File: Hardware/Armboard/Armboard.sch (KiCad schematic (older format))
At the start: 24 parts

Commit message: Added more footprints
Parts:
- Conn1, Conn2: footprint (none) -> MRDT_Connectors:Anderson_1_Horizontal
- Conn3, Conn4, Conn5: footprint (none) -> MRDT_Connectors:Anderson_3_Vertical_Side_by_Side
- Conn6, Conn7: footprint (none) -> MRDT_Connectors:Anderson_2_Vertical_Sidy_by_Side
- D2, D3, D4, D5, D6, D7: footprint (none) -> LED_SMD:LED_0603_1608Metric_Pad1.05x0.95mm_HandSolder
- FB1, FB2, FB3, FB4, FB5: footprint (none) -> Capacitor_SMD:C_0805_2012Metric_Pad1.15x1.40mm_HandSolder
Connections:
- net Power/12V is gone; now on net Power/12V: Conn2.2 (V+Log), Conn3.2 (V+Log), Conn4.2 (V+Log), Conn5.2 (V+Log)
- net Power/12V: no longer FB1.2, FB2.2, FB3.2
- new net Power/12V: FB1.2, FB2.2, FB3.2
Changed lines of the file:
@@
 F 0 "Conn1" H 1843 1737 60  0000 C CNN
 F 1 "AndersonPP" H 1843 1631 60  0000 C CNN
-F 2 "" H 1485 800 60  0001 C CNN
+F 2 "MRDT_Connectors:Anderson_1_Horizontal" H 1485 800 60  0001 C CNN
 F 3 "" H 1485 800 60  0001 C CNN
 	3    1635 1350
@@
 F 0 "D2" H 9608 1357 50  0000 C CNN
 F 1 "LED" H 9608 1266 50  0000 C CNN
-F 2 "" H 9615 1520 50  0001 C CNN
+F 2 "LED_SMD:LED_0603_1608Metric_Pad1.05x0.95mm_HandSolder" H 9615 1520 50  0001 C CNN
 F 3 "~" H 9615 1520 50  0001 C CNN
 	1    9615 1520
@@
 F 0 "Conn6" H 10340 1750 60  0000 R CNN
 F 1 "AndersonPP" H 10440 1650 60  0000 R CNN
-F 2 "" H 9890 800 60  0001 C CNN
+F 2 "MRDT_Connectors:Anderson_2_Vertical_Sidy_by_Side" H 9890 800 60  0001 C CNN
 F 3 "" H 9890 800 60  0001 C CNN
 	2    10040 1350
@@
 F 0 "D6" H 4718 1140 50  0000 C CNN
 F 1 "LED" H 4718 1231 50  0000 C CNN
-F 2 "" H 4725 1395 50  0001 C CNN
+F 2 "LED_SMD:LED_0603_1608Metric_Pad1.05x0.95mm_HandSolder" H 4725 1395 50  0001 C CNN
 F 3 "~" H 4725 1395 50  0001 C CNN
 	1    4725 1395
@@
 F 0 "Conn3" H 1425 2950 60  0000 C CNN
 F 1 "AndersonPP" H 1330 2840 60  0000 C CNN
-F 2 "" H 1485 2240 60  0001 C CNN
+F 2 "MRDT_Connectors:Anderson_3_Vertical_Side_by_Side" H 1485 2240 60  0001 C CNN
 F 3 "" H 1485 2240 60  0001 C CNN
 	1    1635 2790
@@
 F 0 "Conn4" H 1425 3175 60  0000 C CNN
 F 1 "AndersonPP" H 1330 3065 60  0000 C CNN
-F 2 "" H 1485 2465 60  0001 C CNN
+F 2 "MRDT_Connectors:Anderson_3_Vertical_Side_by_Side" H 1485 2465 60  0001 C CNN
 F 3 "" H 1485 2465 60  0001 C CNN
 	1    1635 3015
@@
 F 0 "Conn5" H 1425 3400 60  0000 C CNN
 F 1 "AndersonPP" H 1330 3290 60  0000 C CNN
-F 2 "" H 1485 2690 60  0001 C CNN
+F 2 "MRDT_Connectors:Anderson_3_Vertical_Side_by_Side" H 1485 2690 60  0001 C CNN
 F 3 "" H 1485 2690 60  0001 C CNN
 	1    1635 3240
@@
 F 0 "Conn2" H 1425 2725 60  0000 C CNN
 F 1 "AndersonPP" H 1330 2615 60  0000 C CNN
-F 2 "" H 1485 2015 60  0001 C CNN
+F 2 "MRDT_Connectors:Anderson_1_Horizontal" H 1485 2015 60  0001 C CNN
 F 3 "" H 1485 2015 60  0001 C CNN
 	1    1635 2565
@@
 F 0 "FB4" V 8898 1250 50  0000 C CNN
 F 1 "Ferrite_Bead_Small" V 8989 1250 50  0000 C CNN
-F 2 "" V 9065 1250 50  0001 C CNN
+F 2 "Capacitor_SMD:C_0805_2012Metric_Pad1.15x1.40mm_HandSolder" V 9065 1250 50  0001 C CNN
 F 3 "~" H 9135 1250 50  0001 C CNN
 	1    9135 1250
@@
 F 0 "D7" H 9728 2407 50  0000 C CNN
 F 1 "LED" H 9728 2316 50  0000 C CNN
-F 2 "" H 9735 2570 50  0001 C CNN
+F 2 "LED_SMD:LED_0603_1608Metric_Pad1.05x0.95mm_HandSolder" H 9735 2570 50  0001 C CNN
 F 3 "~" H 9735 2570 50  0001 C CNN
 	1    9735 2570
@@
 F 0 "Conn7" H 10480 2800 60  0000 R CNN
 F 1 "AndersonPP" H 10580 2700 60  0000 R CNN
-F 2 "" H 10030 1850 60  0001 C CNN
+F 2 "MRDT_Connectors:Anderson_2_Vertical_Sidy_by_Side" H 10030 1850 60  0001 C CNN
 F 3 "" H 10030 1850 60  0001 C CNN
 	2    10180 2400
@@
 F 0 "FB5" V 9038 2300 50  0000 C CNN
 F 1 "Ferrite_Bead_Small" V 9129 2300 50  0000 C CNN
-F 2 "" V 9205 2300 50  0001 C CNN
+F 2 "Capacitor_SMD:C_0805_2012Metric_Pad1.15x1.40mm_HandSolder" V 9205 2300 50  0001 C CNN
 F 3 "~" H 9275 2300 50  0001 C CNN
 	1    9275 2300
@@
 F 0 "FB1" V 4125 1805 30  0000 C CNN
 F 1 "Ferrite_Bead_Small" V 4190 1805 30  0000 C CNN
-F 2 "" V 4225 1805 50  0001 C CNN
+F 2 "Capacitor_SMD:C_0805_2012Metric_Pad1.15x1.40mm_HandSolder" V 4225 1805 50  0001 C CNN
 F 3 "~" H 4295 1805 50  0001 C CNN
 	1    4295 1805
@@
 F 0 "D3" H 4715 2150 30  0000 C CNN
 F 1 "LED" H 4630 2150 30  0000 C CNN
-F 2 "" H 4655 2005 50  0001 C CNN
+F 2 "LED_SMD:LED_0603_1608Metric_Pad1.05x0.95mm_HandSolder" H 4655 2005 50  0001 C CNN
 F 3 "~" H 4655 2005 50  0001 C CNN
 	1    4655 2005
@@
 F 0 "Conn2" H 4962 1752 60  0000 R CNN
 F 1 "AndersonPP" H 4962 1858 60  0000 R CNN
-F 2 "" H 4840 1155 60  0001 C CNN
+F 2 "MRDT_Connectors:Anderson_1_Horizontal" H 4840 1155 60  0001 C CNN
 F 3 "" H 4840 1155 60  0001 C CNN
 	3    4990 1705
@@
 F 0 "FB2" V 4175 2265 30  0000 C CNN
 F 1 "Ferrite_Bead_Small" V 4225 2310 30  0000 C CNN
-F 2 "" V 4255 2220 50  0001 C CNN
+F 2 "Capacitor_SMD:C_0805_2012Metric_Pad1.15x1.40mm_HandSolder" V 4255 2220 50  0001 C CNN
 F 3 "~" H 4325 2220 50  0001 C CNN
 	1    4325 2220
@@
 F 0 "D4" H 4685 2555 30  0000 C CNN
 F 1 "LED" H 4685 2320 30  0000 C CNN
-F 2 "" H 4685 2420 50  0001 C CNN
+F 2 "LED_SMD:LED_0603_1608Metric_Pad1.05x0.95mm_HandSolder" H 4685 2420 50  0001 C CNN
 F 3 "~" H 4685 2420 50  0001 C CNN
 	1    4685 2420
@@
 F 0 "Conn3" H 4992 2167 60  0000 R CNN
 F 1 "AndersonPP" H 4992 2273 60  0000 R CNN
-F 2 "" H 4870 1570 60  0001 C CNN
+F 2 "MRDT_Connectors:Anderson_3_Vertical_Side_by_Side" H 4870 1570 60  0001 C CNN
 F 3 "" H 4870 1570 60  0001 C CNN
 	3    5020 2120
@@
 F 0 "FB3" V 4175 2725 30  0000 C CNN
 F 1 "Ferrite_Bead_Small" V 4225 2770 30  0000 C CNN
-F 2 "" V 4255 2680 50  0001 C CNN
+F 2 "Capacitor_SMD:C_0805_2012Metric_Pad1.15x1.40mm_HandSolder" V 4255 2680 50  0001 C CNN
 F 3 "~" H 4325 2680 50  0001 C CNN
 	1    4325 2680
@@
 F 0 "D5" H 4685 3015 30  0000 C CNN
 F 1 "LED" H 4685 2780 30  0000 C CNN
-F 2 "" H 4685 2880 50  0001 C CNN
+F 2 "LED_SMD:LED_0603_1608Metric_Pad1.05x0.95mm_HandSolder" H 4685 2880 50  0001 C CNN
 F 3 "~" H 4685 2880 50  0001 C CNN
 	1    4685 2880
@@
 F 0 "Conn4" H 4992 2627 60  0000 R CNN
 F 1 "AndersonPP" H 4992 2733 60  0000 R CNN
-F 2 "" H 4870 2030 60  0001 C CNN
+F 2 "MRDT_Connectors:Anderson_3_Vertical_Side_by_Side" H 4870 2030 60  0001 C CNN
 F 3 "" H 4870 2030 60  0001 C CNN
 	3    5020 2580
@@
 F 0 "Conn2" H 1450 1750 60  0000 C CNN
 F 1 "AndersonPP" H 1355 1655 60  0000 C CNN
-F 2 "" H 1485 1060 60  0001 C CNN
+F 2 "MRDT_Connectors:Anderson_1_Horizontal" H 1485 1060 60  0001 C CNN
 F 3 "" H 1485 1060 60  0001 C CNN
 	2    1635 1610
@@
 F 0 "Conn3" H 1450 1975 60  0000 C CNN
 F 1 "AndersonPP" H 1355 1880 60  0000 C CNN
-F 2 "" H 1485 1285 60  0001 C CNN
+F 2 "MRDT_Connectors:Anderson_3_Vertical_Side_by_Side" H 1485 1285 60  0001 C CNN
 F 3 "" H 1485 1285 60  0001 C CNN
 	2    1635 1835
@@
 F 0 "Conn4" H 1450 2200 60  0000 C CNN
 F 1 "AndersonPP" H 1355 2105 60  0000 C CNN
-F 2 "" H 1485 1510 60  0001 C CNN
+F 2 "MRDT_Connectors:Anderson_3_Vertical_Side_by_Side" H 1485 1510 60  0001 C CNN
 F 3 "" H 1485 1510 60  0001 C CNN
 	2    1635 2060
@@
 F 0 "Conn5" H 1450 2425 60  0000 C CNN
 F 1 "AndersonPP" H 1355 2330 60  0000 C CNN
-F 2 "" H 1485 1735 60  0001 C CNN
+F 2 "MRDT_Connectors:Anderson_3_Vertical_Side_by_Side" H 1485 1735 60  0001 C CNN
 F 3 "" H 1485 1735 60  0001 C CNN
 	2    1635 2285

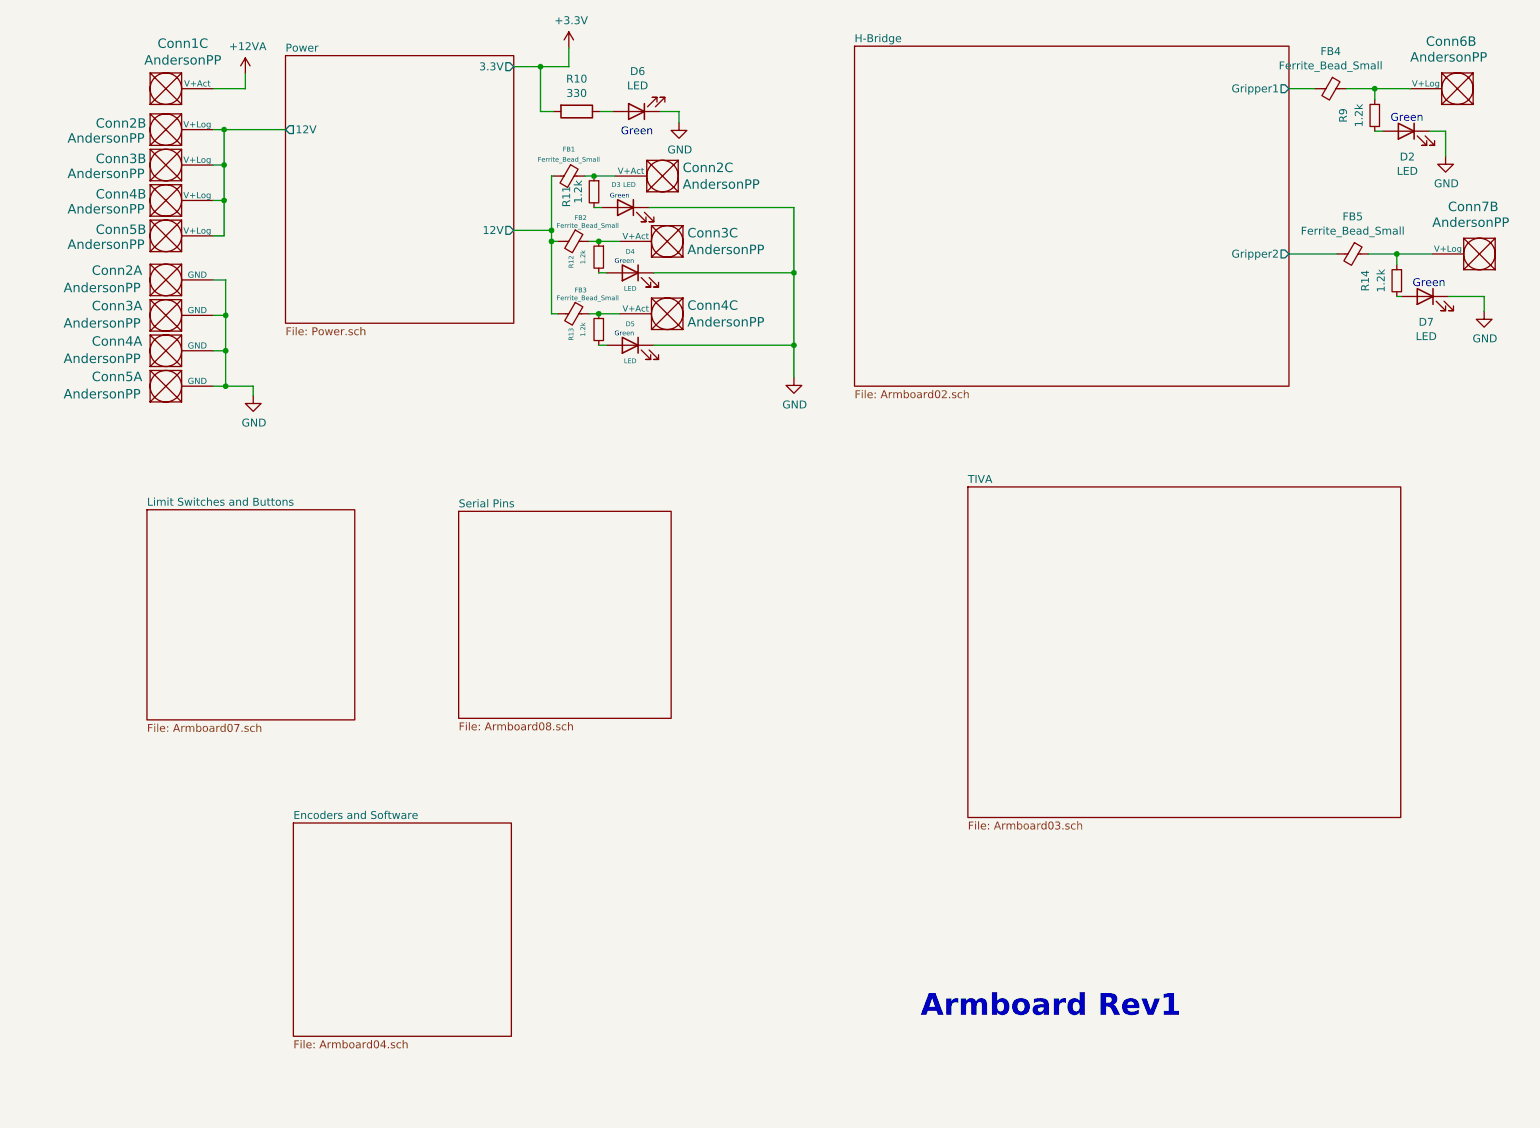
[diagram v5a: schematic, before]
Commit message: Fixed Andersons, made netlist, imported footprints to layout
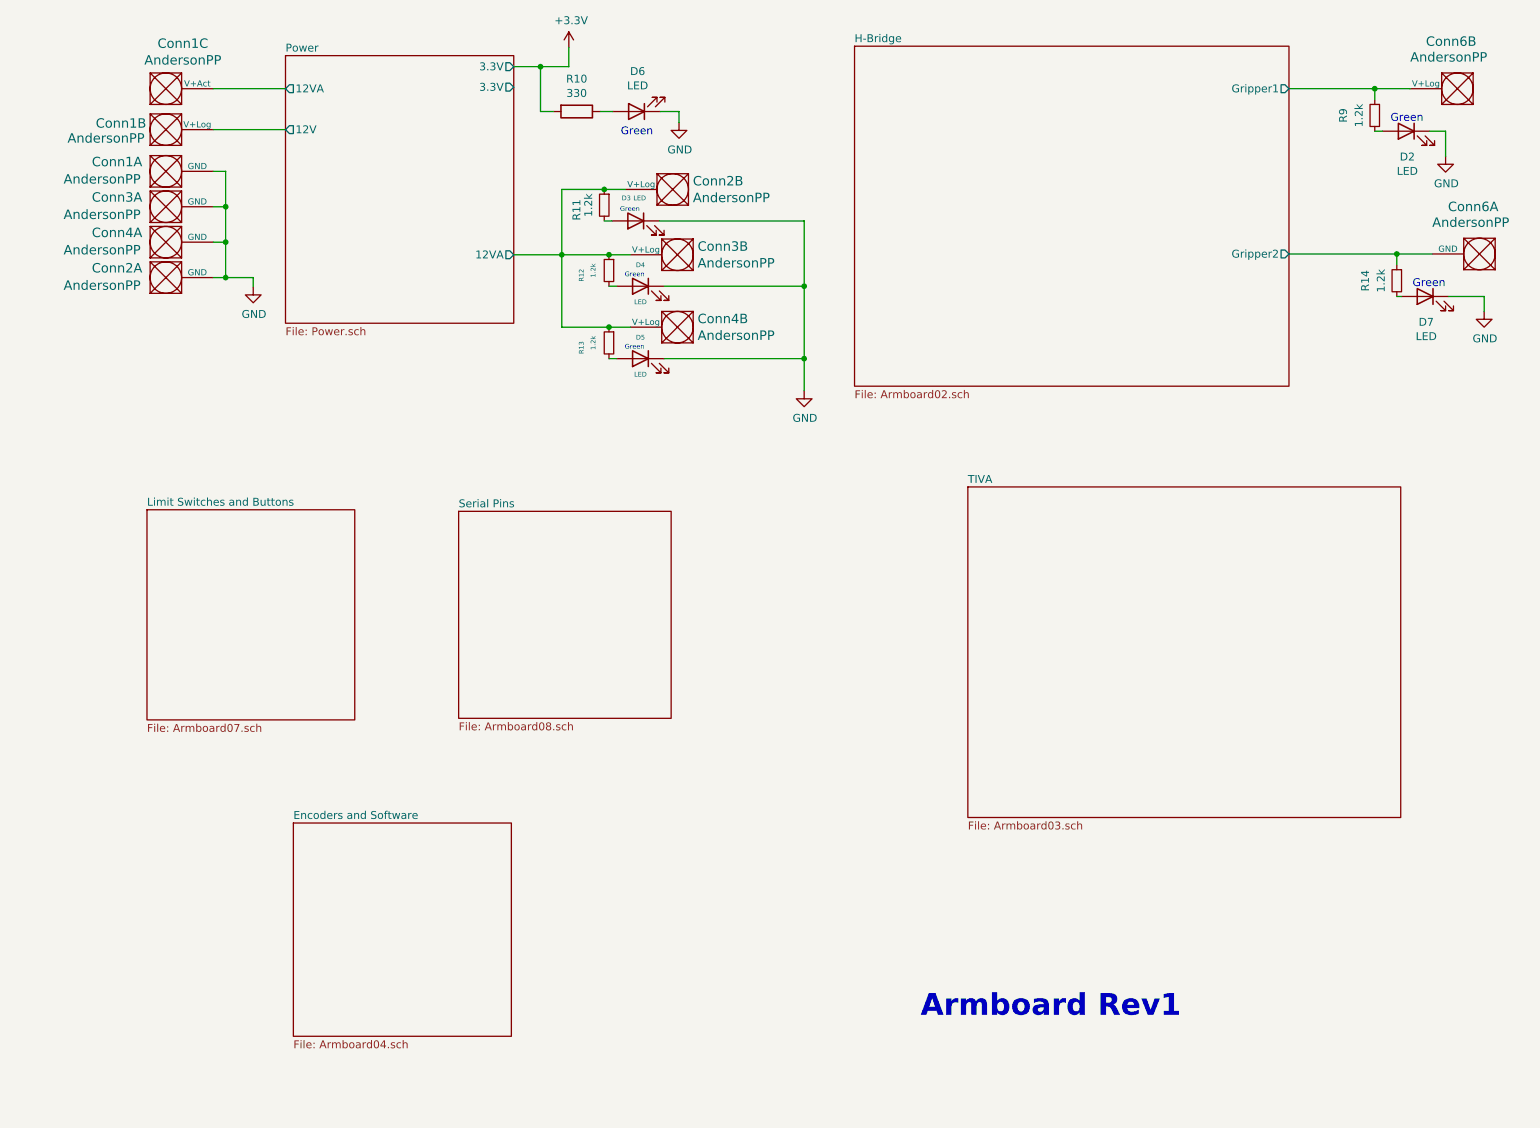
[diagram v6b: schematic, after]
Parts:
- removed unit 2 of Conn3
- removed unit 2 of Conn4
- removed unit 2 of Conn5
- removed FB1, FB2, FB3, FB4, FB5: Ferrite_Bead_Small, Capacitor_SMD:C_0805_2012Metric_Pad1.15x1.40mm_HandSolder, symbol Device:Ferrite_Bead_Small
- Conn1: footprint MRDT_Connectors:Anderson_1_Horizontal -> MRDT_Connectors:Anderson_3_Horizontal_Side_by_Side
- Conn1: renamed from Conn2; footprint MRDT_Connectors:Anderson_1_Horizontal -> MRDT_Connectors:Anderson_3_Horizontal_Side_by_Side
- Conn2: footprint MRDT_Connectors:Anderson_1_Horizontal -> MRDT_Connectors:Anderson_2_Vertical_Sidy_by_Side
- Conn2: renamed from Conn5; footprint MRDT_Connectors:Anderson_3_Vertical_Side_by_Side -> MRDT_Connectors:Anderson_2_Vertical_Sidy_by_Side
- Conn3, Conn4: footprint MRDT_Connectors:Anderson_3_Vertical_Side_by_Side -> MRDT_Connectors:Anderson_2_Vertical_Sidy_by_Side
- renumbered Conn7 to Conn6
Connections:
- net Power/12V is gone; now on net Power/12V: Conn1.2 (V+Log)
- net H-Bridge/Gripper1: now also Conn6.2 (V+Log), R9.1
- net H-Bridge/Gripper2: now also Conn6.1 (GND), R14.1
- net Power/12VA: now reaches R11.1
- net Power/12VA: now also Conn2.2 (V+Log), Conn3.2 (V+Log), Conn4.2 (V+Log), R12.1, R13.1; no longer Conn2.3 (V+Act)
- net +12VA renamed Power/12VA
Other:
- moved on the sheet: Conn1A, Conn2A, Conn3A, Conn4A, D3, D4, D5, R11, R12, R13

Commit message: Double-checked schematic, pointed power pins up, made sure 12V and 3.3V were full networks
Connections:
- net Power/12VA is gone; now on net Power/12VA: Conn2.2 (V+Log), Conn3.2 (V+Log), Conn4.2 (V+Log), R11.1, R12.1, R13.1
- net Power/12VA: no longer Conn1.3 (V+Act)
- new net Power/12VA: Conn1.3 (V+Act)
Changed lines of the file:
@@
 F0 "Power" 50
 F1 "Power.sch" 50
-F2 "3.3V" O R 3945 1240 50
-F3 "12V" O L 2495 1510 50
-F4 "12VA" O L 2495 1250 50
-F5 "12VA" O R 3945 2305 50
-F6 "3.3V" O R 3945 1110 50
+F2 "12V" O L 2495 1510 50
+F3 "12VA" O L 2495 1250 50
+F4 "12VA" O R 3945 2305 50
+F5 "3.3V" O R 3945 1110 50
+F6 "12V" O R 3945 1760 50
 $EndSheet
 $Comp
@@
 Wire Wire Line
 	3945 2305 4250 2305
+Wire Wire Line
+	3945 1760 4120 1760
+Wire Wire Line
+	4120 1760 4120 1705
+$Comp
+L power:+12V #PWR0101
+U 1 1 5FBDA204
+P 4120 1705
+F 0 "#PWR0101" H 4120 1555 50  0001 C CNN
+F 1 "+12V" H 4135 1878 50  0000 C CNN
+F 2 "" H 4120 1705 50  0001 C CNN
+F 3 "" H 4120 1705 50  0001 C CNN
+	1    4120 1705
+	1    0    0    -1
+$EndComp
 $EndSCHEMATC

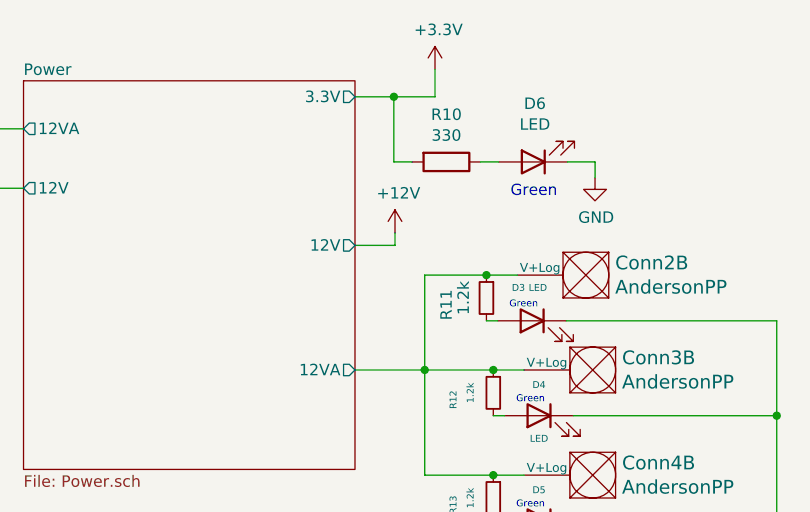
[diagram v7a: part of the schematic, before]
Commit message: Added more labels, fixed 12VA/12L connections, filled gnd islands, +/-/S labels, added drillhole footprints
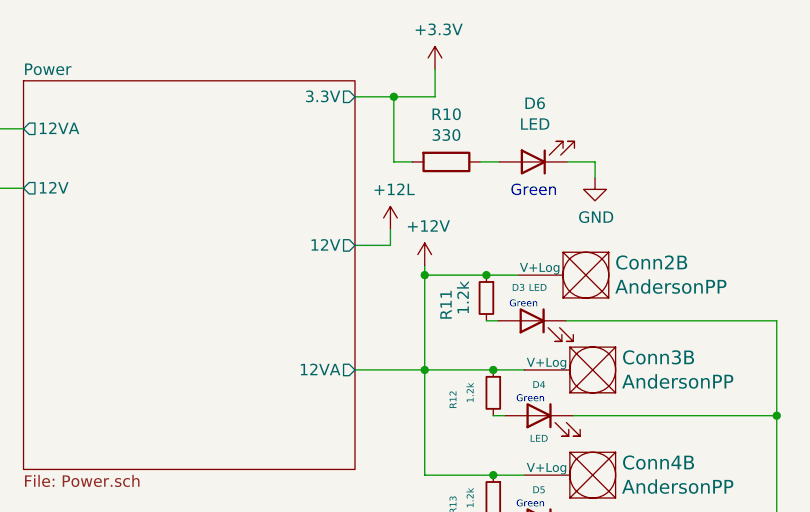
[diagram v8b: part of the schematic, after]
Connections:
- net Power/12VA is gone; now on net +12V: Conn2.2 (V+Log), Conn3.2 (V+Log), Conn4.2 (V+Log), R11.1, R12.1, R13.1
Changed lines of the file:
@@
 Wire Wire Line
 	3945 2305 4250 2305
-Wire Wire Line
-	3945 1760 4120 1760
-Wire Wire Line
-	4120 1760 4120 1705
 $Comp
 L power:+12V #PWR0101
 U 1 1 5FBDA204
-P 4120 1705
-F 0 "#PWR0101" H 4120 1555 50  0001 C CNN
-F 1 "+12V" H 4135 1878 50  0000 C CNN
-F 2 "" H 4120 1705 50  0001 C CNN
-F 3 "" H 4120 1705 50  0001 C CNN
-	1    4120 1705
+P 4250 1850
+F 0 "#PWR0101" H 4250 1700 50  0001 C CNN
+F 1 "+12V" H 4265 2023 50  0000 C CNN
+F 2 "" H 4250 1850 50  0001 C CNN
+F 3 "" H 4250 1850 50  0001 C CNN
+	1    4250 1850
 	1    0    0    -1
 $EndComp
+$Comp
+L power:+12L #PWR?
+U 1 1 5FB940AC
+P 4100 1690
+F 0 "#PWR?" H 4100 1540 50  0001 C CNN
+F 1 "+12L" H 4115 1863 50  0000 C CNN
+F 2 "" H 4100 1690 50  0001 C CNN
+F 3 "" H 4100 1690 50  0001 C CNN
+	1    4100 1690
+	1    0    0    -1
+$EndComp
+Wire Wire Line
+	3945 1760 4100 1760
+Wire Wire Line
+	4250 1890 4250 1850
+Connection ~ 4250 1890
+Wire Wire Line
+	4100 1760 4100 1690
 $EndSCHEMATC
